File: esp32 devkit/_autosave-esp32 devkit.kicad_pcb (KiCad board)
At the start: 2 copper layers, 87.5 x 50.5 mm, 38 parts, among them J1 Conn_01x19, J2 Conn_01x19, Q1 SS8050, Q2 SS8050, SW1 SW_Push, SW2 SW_Push, U1 AMS1117-3.3, U2 ESP32-WROOM-32E(4MB), U4 CP2102N-A02-GQFN28

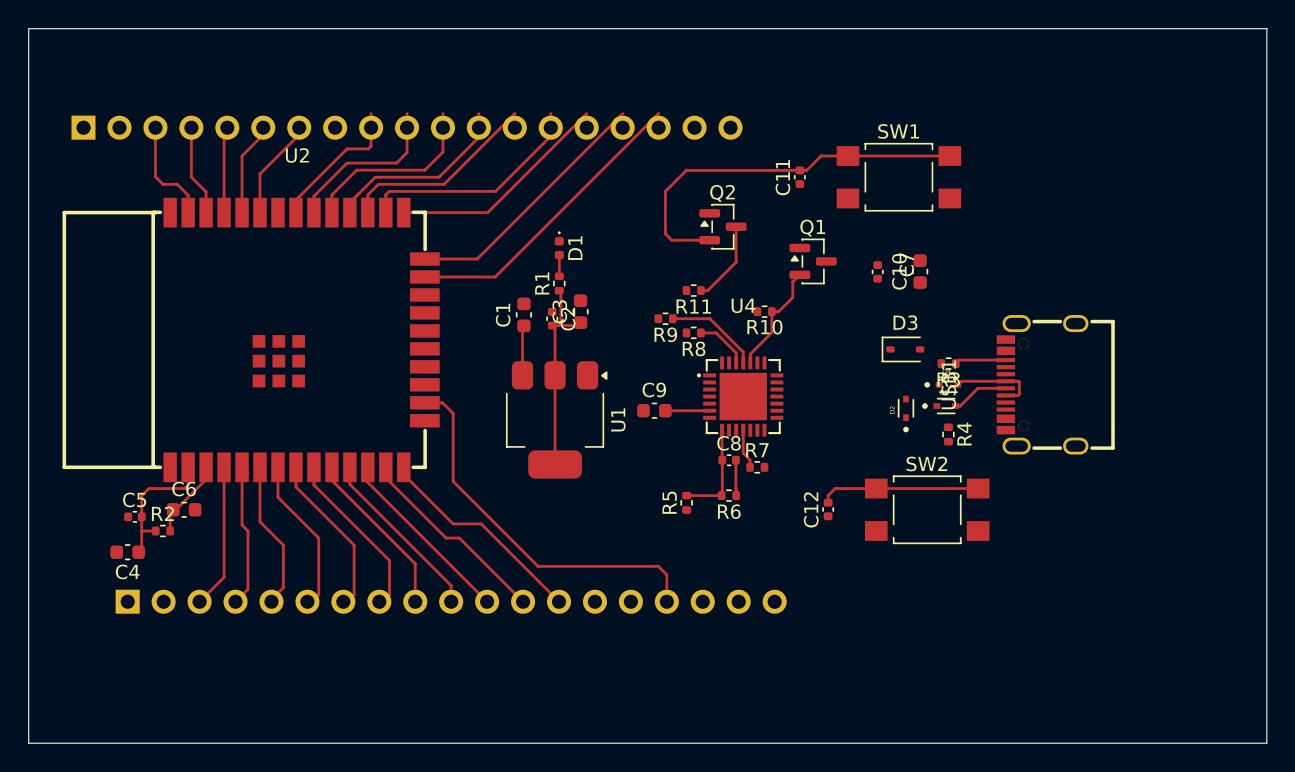
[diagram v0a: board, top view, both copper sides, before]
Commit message: :tada:Completed grounding in filled zones and wiring at the editor
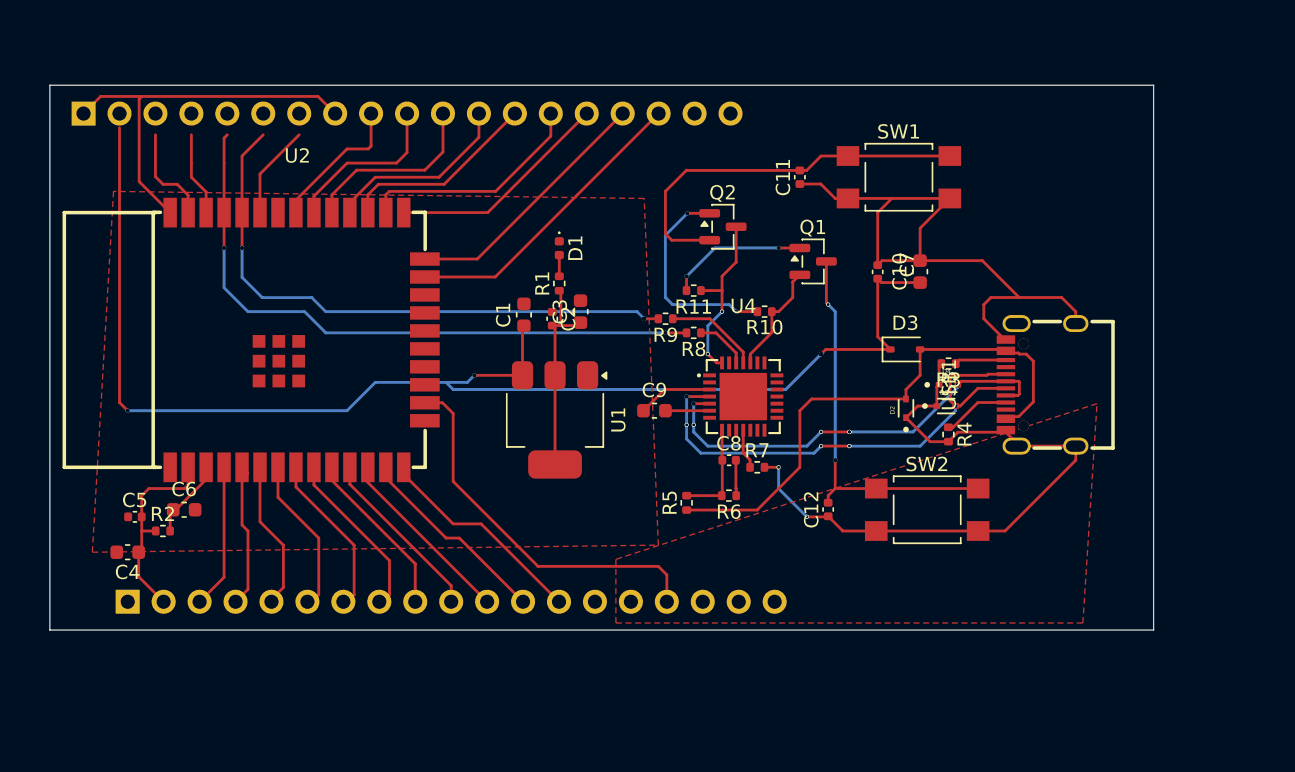
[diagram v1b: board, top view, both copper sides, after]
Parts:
- moved J2 1.00 mm to (18.9, 114.0)
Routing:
- net GND: track 0.00 -> 124.5 mm, vias 0 -> 2
- net VCC: track 3.54 -> 94.0 mm, vias 0 -> 4
- net /TXD0: track 5.60 -> 44.9 mm, vias 0 -> 2
- net VBUS: track 0.00 -> 38.3 mm
- net /RXD0: track 6.12 -> 41.3 mm, vias 0 -> 3
- net /USB_P: track 4.08 -> 35.9 mm, vias 0 -> 5
- net /USB_N: track 6.32 -> 30.4 mm, vias 0 -> 6
- net /CHIP_EN: track 17.0 -> 33.3 mm, vias 0 -> 2
- net Net-(Q2-B): track 0.00 -> 15.1 mm, vias 0 -> 2
- net Net-(Q1-B): track 0.00 -> 9.84 mm, vias 0 -> 2
- net /DTR: track 5.82 -> 12.6 mm, vias 0 -> 2
- net Net-(USB1-CC1): track 0.00 -> 4.78 mm
- net +3.3V: track 27.5 -> 31.7 mm
- added copper zone on F.Cu, net GND
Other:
- board size 87.5 x 50.5 mm -> 78 x 38.5 mm
